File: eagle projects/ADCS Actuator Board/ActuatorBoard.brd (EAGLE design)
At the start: 91 x 91 mm, 228 parts, among them J11 TE_1-84953-1, J2 TE_1-84953-1, J4 TE_1-84953-1, J5 TE-1734829-3, U1 SIP2100DY-T1-GE3, U10 LM2917MX/NOPB, U12 TSV991AILT, U13 LM2917MX/NOPB, U14 ADS7841E_2K5, U16 DRV10970_MOTOR_DRIVERDRV10970, U17 LM2917MX/NOPB, U19 TSV991AILT, U2 SIP2100DY-T1-GE3, U20 ADS7841E_2K5, U3 SIP2100DY-T1-GE3, U6 DRV10970_MOTOR_DRIVERDRV10970, U7 DRV10970_MOTOR_DRIVERDRV10970, U8 TSV991AILT, U9 ADS7841E_2K5

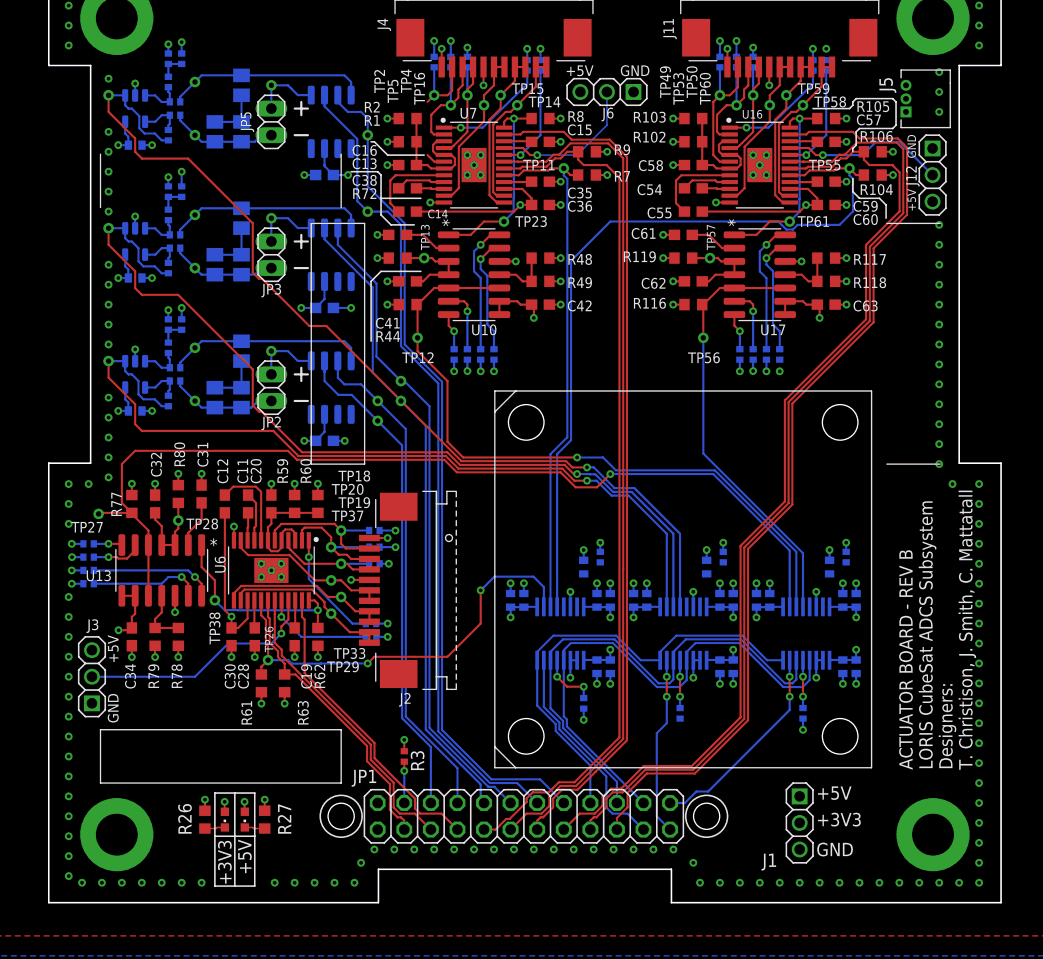
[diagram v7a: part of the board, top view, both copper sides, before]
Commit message: Silkscreen updates
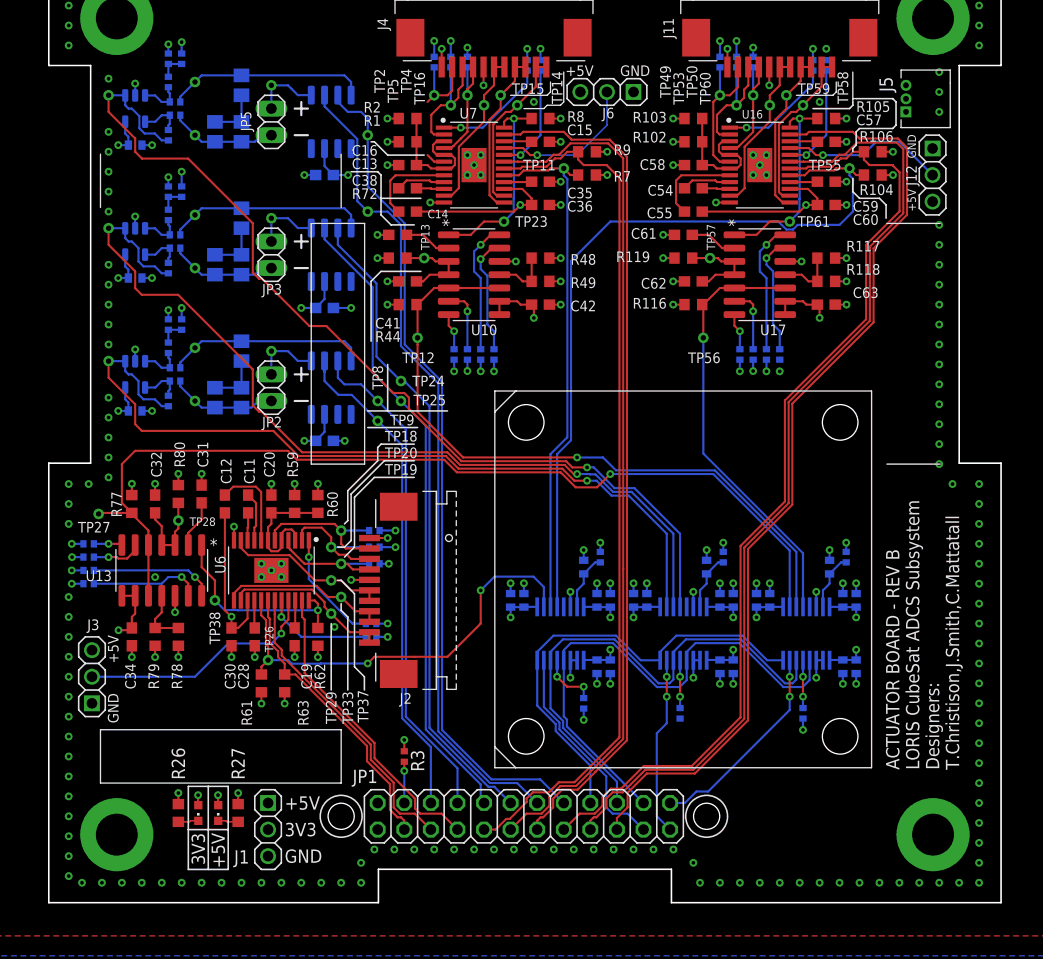
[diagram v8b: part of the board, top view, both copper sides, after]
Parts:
- R11, R22, R24, R30, R42, R47, R82, R88, R89: device rcl:M0805 -> rcl:R0805
- moved J1 50.8 mm to (21.0, 6.99)
- moved LED2 2.62 mm to (16.2, 8.57)
- moved LED1 2.62 mm to (14.3, 8.57)
- moved R26 2.62 mm to (12.4, 8.57)
- moved R27 2.62 mm to (18.1, 8.57)
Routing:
- net N$2: track 0.00 -> 5.45 mm
- net N$7: track 0.00 -> 5.45 mm
- net N$4: track 0.00 -> 5.45 mm
- net CUR_OUT3: track 92.1 -> 92.7 mm
- net GND: vias 293 -> 300
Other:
- board text added: "3V3"
- board text added: "T.Christison,J.Smith,C.Mattatall"
- board text removed: "+3V3"
- board text removed: "T. Christison, J. Smith, C. Mattatall"
